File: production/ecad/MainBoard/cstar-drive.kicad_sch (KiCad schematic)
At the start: 55 parts, among them J1 B4B-PH-K-S, J2 B4B-PH-K-S, J3 Conn_01x03_Pin, J4 Conn_01x03_Pin, J5 Conn_01x03_Pin, J6 Conn_01x03_Pin, J7 Conn_01x03_Pin, J8 Conn_01x03_Pin, J9 Conn_01x03_Pin, U1 DRV8842PWPR, U2 DRV8842PWPR, X1 B2P-VH, X2 B2P-VH

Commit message: drive footprints (0805 C, R, connector pins)
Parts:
- C1, C10, C11, C12, C2, C3, C4, C5, C6, C7, C8, C9: footprint (none) -> Capacitor_SMD:C_0805_2012Metric
- J3, J4, J5, J6, J7, J8, J9: footprint (none) -> Connector_Phoenix_SPT:PhoenixContact_SPT_1.5_9-H-3.5_1x09_P3.5mm_Horizontal
- R1, R10, R2, R3, R4, R5, R6, R7, R8, R9: footprint (none) -> Resistor_SMD:R_0805_2012Metric

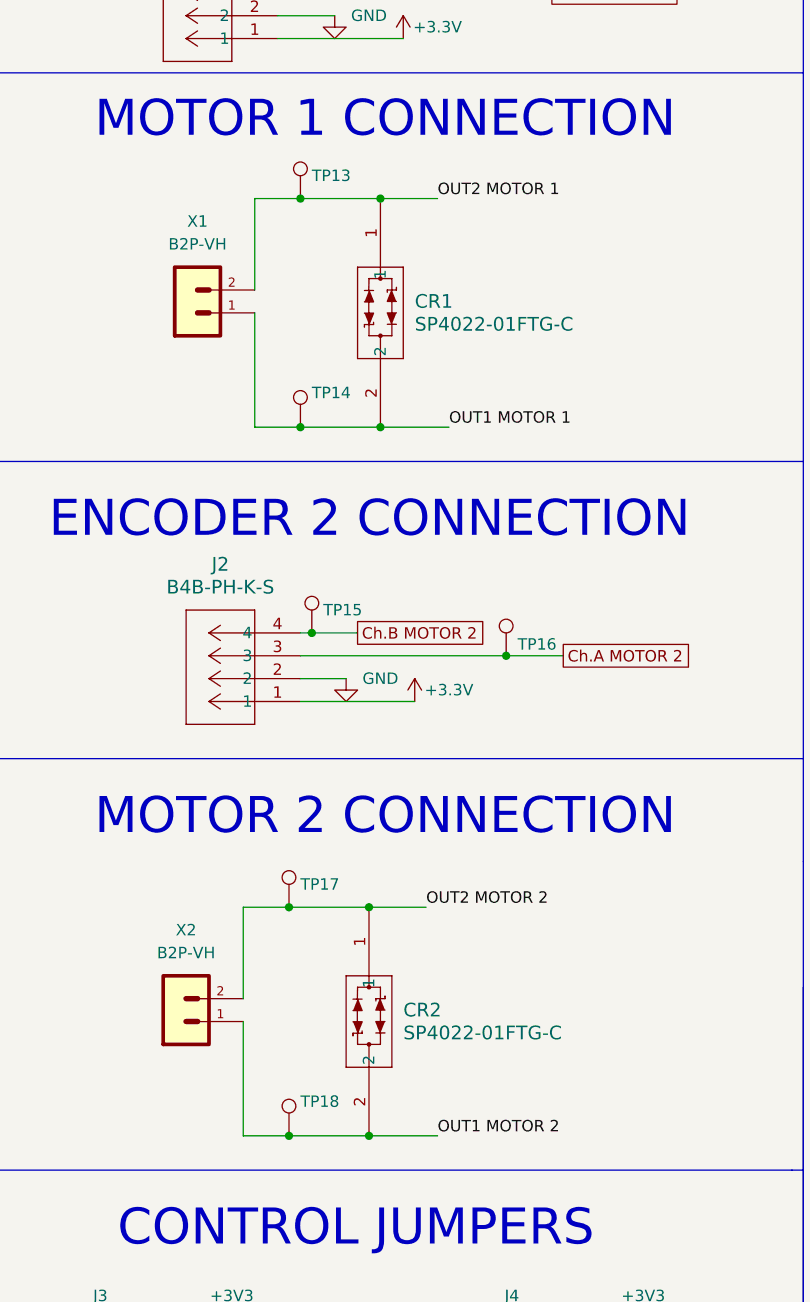
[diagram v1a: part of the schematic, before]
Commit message: "Added TP Footprints for drive"
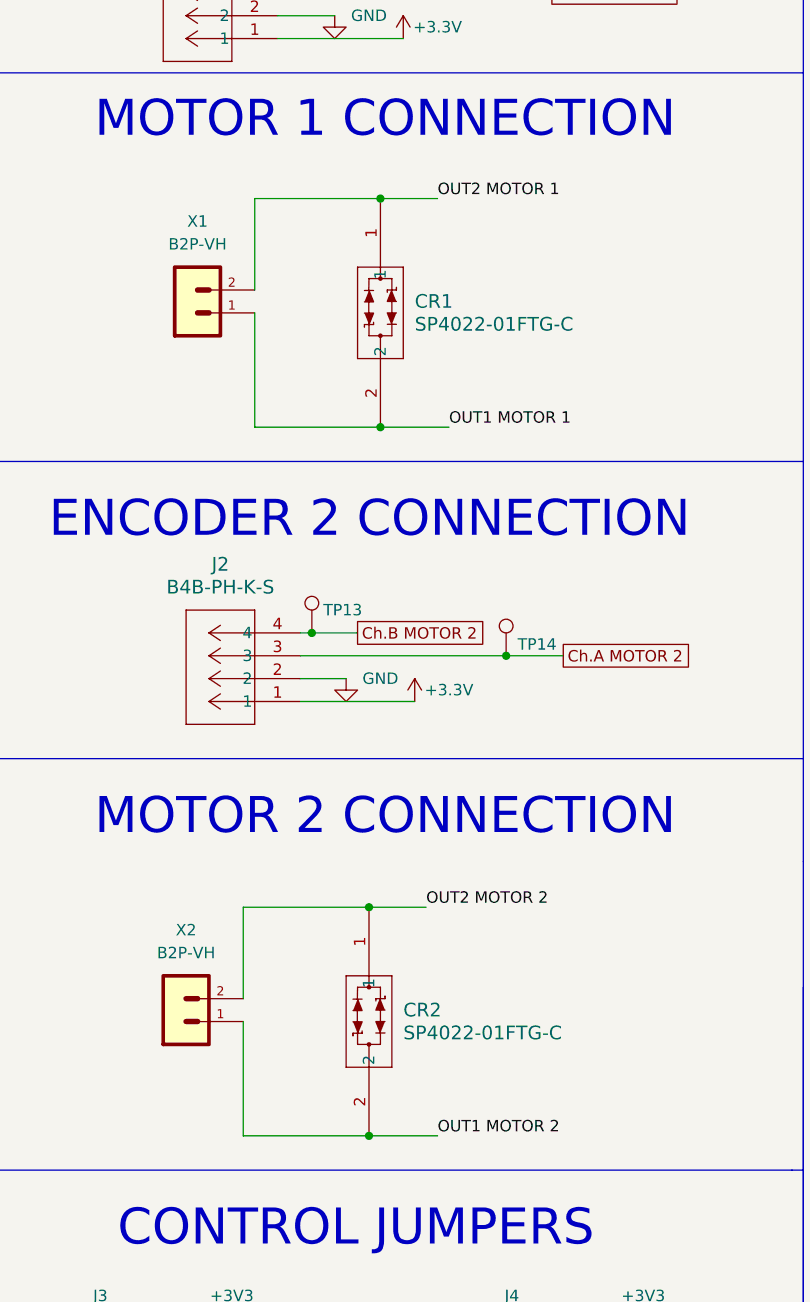
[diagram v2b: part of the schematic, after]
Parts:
- removed TP13, TP17: OUT2 MOTOR 1 TP, symbol Connector:TestPoint
- removed TP14, TP18: ~, symbol Connector:TestPoint
- TP1: footprint (none) -> TestPoint:TestPoint_Pad_D1.5mm
- TP10: value IN1 MOTOR 1 TP -> OUT2 MOTOR 2 TP; footprint (none) -> TestPoint:TestPoint_Pad_D1.5mm
- TP11: value TestPoint -> Ch.B MOTOR 1; footprint (none) -> TestPoint:TestPoint_Pad_D1.5mm
- TP12: value TestPoint -> Ch.A MOTOR 1; footprint (none) -> TestPoint:TestPoint_Pad_D1.5mm
- TP13: renamed from TP15; value TestPoint -> Ch.B MOTOR 2 TP; footprint (none) -> TestPoint:TestPoint_Pad_D1.5mm
- TP14: renamed from TP16; value TestPoint -> Ch.A MOTOR 2; footprint (none) -> TestPoint:TestPoint_Pad_D1.5mm
- TP2: value IN1 MOTOR 1 TP -> IN2 MOTOR 1 TP; footprint (none) -> TestPoint:TestPoint_Pad_D1.5mm; now left out of the parts list
- TP3: value IN1 MOTOR 1 TP -> nFAULT MOTOR 1 TP; footprint (none) -> TestPoint:TestPoint_Pad_D1.5mm
- TP4: value IN1 MOTOR 1 TP -> OUT1 MOTOR 1 TP; footprint (none) -> TestPoint:TestPoint_Pad_D1.5mm
- TP5: value IN1 MOTOR 1 TP -> OUT2 MOTOR 1 TP; footprint (none) -> TestPoint:TestPoint_Pad_D1.5mm
- TP6: value IN1 MOTOR 1 TP -> IN1 MOTOR 2 TP; footprint (none) -> TestPoint:TestPoint_Pad_D1.5mm
- TP7: value IN1 MOTOR 1 TP -> IN2 MOTOR 2 TP; footprint (none) -> TestPoint:TestPoint_Pad_D1.5mm
- TP8: value IN1 MOTOR 1 TP -> nFAULT MOTOR 2 TP; footprint (none) -> TestPoint:TestPoint_Pad_D1.5mm
- TP9: value IN1 MOTOR 1 TP -> OUT1 MOTOR 2 TP; footprint (none) -> TestPoint:TestPoint_Pad_D1.5mm

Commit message: "Added Footprints and Datasheets for all components in Drive Schematic"
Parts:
- CR1, CR2: footprint ZDO_SP4022_LTF -> SP4022_01FTG_C:ZDO_SP4022_LTF
- J1, J2: footprint CONN4_B4B-PH_JST -> B4B_PH_K_S:B4B_PH_K_S
- U1, U2: footprint PWP0028C_N -> DRV8842PWPR:PWP0028C_N
- X1, X2: footprint (none) -> B2P-VH:B2P-VH
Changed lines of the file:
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@@
       (effects (font (size 1.524 1.524)))
     )
-    (property "Footprint" "CONN4_B4B-PH_JST" (at 223.52 62.23 0)
+    (property "Footprint" "B4B_PH_K_S:B4B_PH_K_S" (at 223.52 62.23 0)
       (effects (font (size 1.27 1.27) italic) hide)
     )
-    (property "Datasheet" "B4B-PH-K-S" (at 223.52 62.23 0)
+    (property "Datasheet" "https://www.jst-mfg.com/product/pdf/eng/ePH.pdf" (at 223.52 62.23 0)
       (effects (font (size 1.27 1.27) italic) hide)
     )
@@
       (effects (font (size 1.524 1.524)) (justify left))
     )
-    (property "Footprint" "ZDO_SP4022_LTF" (at 233.68 158.75 0)
+    (property "Footprint" "SP4022_01FTG_C:ZDO_SP4022_LTF" (at 233.68 158.75 0)
       (effects (font (size 1.27 1.27) italic) hide)
     )
@@
       (effects (font (size 1.524 1.524)))
     )
-    (property "Footprint" "PWP0028C_N" (at 113.03 233.68 0)
+    (property "Footprint" "DRV8842PWPR:PWP0028C_N" (at 113.03 233.68 0)
       (effects (font (size 1.27 1.27) italic) hide)
     )
-    (property "Datasheet" "DRV8842PWPR" (at 113.03 233.68 0)
+    (property "Datasheet" "https://www.ti.com/lit/ds/symlink/drv8842.pdf?HQS=dis-dk-null-digikeymode-dsf-pf-null-wwe&ts=1708386124050" (at 113.03 233.68 0)
       (effects (font (size 1.27 1.27) italic) hide)
     )
@@
       (effects (font (size 1.524 1.524)) (justify left))
     )
-    (property "Footprint" "ZDO_SP4022_LTF" (at 234.95 80.01 0)
+    (property "Footprint" "SP4022_01FTG_C:ZDO_SP4022_LTF" (at 234.95 80.01 0)
       (effects (font (size 1.27 1.27) italic) hide)
     )
@@
       (effects (font (size 1.27 1.27)))
     )
-    (property "Footprint" "" (at 212.09 168.91 0)
-      (effects (font (size 1.27 1.27)) hide)
-    )
-    (property "Datasheet" "" (at 212.09 168.91 0)
+    (property "Footprint" "B2P-VH:B2P-VH" (at 212.09 168.91 0)
+      (effects (font (size 1.27 1.27)) hide)
+    )
+    (property "Datasheet" "https://www.jst-mfg.com/product/pdf/eng/eVH.pdf" (at 212.09 168.91 0)
       (effects (font (size 1.27 1.27)) hide)
     )
@@
       (effects (font (size 1.27 1.27)))
     )
-    (property "Footprint" "" (at 213.36 90.17 0)
-      (effects (font (size 1.27 1.27)) hide)
-    )
-    (property "Datasheet" "" (at 213.36 90.17 0)
+    (property "Footprint" "B2P-VH:B2P-VH" (at 213.36 90.17 0)
+      (effects (font (size 1.27 1.27)) hide)
+    )
+    (property "Datasheet" "https://www.jst-mfg.com/product/pdf/eng/eVH.pdf" (at 213.36 90.17 0)
       (effects (font (size 1.27 1.27)) hide)
     )
@@
       (effects (font (size 1.524 1.524)))
     )
-    (property "Footprint" "CONN4_B4B-PH_JST" (at 226.06 135.89 0)
+    (property "Footprint" "B4B_PH_K_S:B4B_PH_K_S" (at 226.06 135.89 0)
       (effects (font (size 1.27 1.27) italic) hide)
     )
-    (property "Datasheet" "B4B-PH-K-S" (at 226.06 135.89 0)
+    (property "Datasheet" "https://www.jst-mfg.com/product/pdf/eng/ePH.pdf" (at 226.06 135.89 0)
       (effects (font (size 1.27 1.27) italic) hide)
     )
@@
       (effects (font (size 1.524 1.524)))
     )
-    (property "Footprint" "PWP0028C_N" (at 111.76 114.3 0)
+    (property "Footprint" "DRV8842PWPR:PWP0028C_N" (at 111.76 114.3 0)
       (effects (font (size 1.27 1.27) italic) hide)
     )
-    (property "Datasheet" "DRV8842PWPR" (at 111.76 114.3 0)
+    (property "Datasheet" "https://www.ti.com/lit/ds/symlink/drv8842.pdf?HQS=dis-dk-null-digikeymode-dsf-pf-null-wwe&ts=1708386124050" (at 111.76 114.3 0)
       (effects (font (size 1.27 1.27) italic) hide)
     )

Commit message: "Updated Net Labels"
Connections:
- net Ch.A MOTOR 1 renamed Ch.A_MOTOR_1
- net Ch.A MOTOR 2 renamed Ch.A_MOTOR_2
- net Ch.B MOTOR 1 renamed Ch.B_MOTOR_1
- net Ch.B MOTOR 2 renamed Ch.B_MOTOR_2
- net IN1 MOTOR 1 renamed IN1_MOTOR_1
- net IN1 MOTOR 2 renamed IN1_MOTOR_2
- net IN2 MOTOR 1 renamed IN2_MOTOR_1
- net IN2 MOTOR 2 renamed IN2_MOTOR_2
- net OUT1 MOTOR 1 renamed OUT1_MOTOR_1
- net OUT1 MOTOR 2 renamed OUT1_MOTOR_2
- net OUT2 MOTOR 1 renamed OUT2_MOTOR_1
- net OUT2 MOTOR 2 renamed OUT2_MOTOR_2
- net nFAULT MOTOR 1 renamed nFAULT_MOTOR_1
- net nFAULT MOTOR 2 renamed nFAULT_MOTOR_2
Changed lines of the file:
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@@
     (stroke (width 0) (type default))
   )
-  (wire (pts (xy 227.33 128.27) (xy 232.41 128.27))
+  (wire (pts (xy 227.33 128.27) (xy 231.14 128.27))
     (stroke (width 0) (type default))
   )
@@
     (stroke (width 0) (type default))
   )
-  (wire (pts (xy 226.06 54.61) (xy 231.14 54.61))
+  (wire (pts (xy 226.06 54.61) (xy 229.87 54.61))
     (stroke (width 0) (type default))
   )
@@
     (effects (font (size 10 10) (thickness 2) bold) (justify left bottom))
   )
-  (label "OUT2 MOTOR 1" (at 241.3 80.01 0) (fields_autoplaced)
+  (label "OUT2_MOTOR_1" (at 241.3 80.01 0) (fields_autoplaced)
     (effects (font (size 1.27 1.27)) (justify left bottom))
   )
@@
     (effects (font (size 1.27 1.27)) (justify left bottom))
   )
-  (label "OUT2 MOTOR 2" (at 240.03 158.75 0) (fields_autoplaced)
+  (label "OUT2_MOTOR_2" (at 240.03 158.75 0) (fields_autoplaced)
     (effects (font (size 1.27 1.27)) (justify left bottom))
   )
@@
     (effects (font (size 1.27 1.27)) (justify left bottom))
   )
-  (label "OUT1 MOTOR 1" (at 143.51 93.98 0) (fields_autoplaced)
-    (effects (font (size 1.27 1.27)) (justify left bottom))
-  )
-  (label "OUT1 MOTOR 2" (at 241.3 184.15 0) (fields_autoplaced)
+  (label "OUT1_MOTOR_1" (at 143.51 93.98 0) (fields_autoplaced)
+    (effects (font (size 1.27 1.27)) (justify left bottom))
+  )
+  (label "OUT1_MOTOR_2" (at 241.3 184.15 0) (fields_autoplaced)
     (effects (font (size 1.27 1.27)) (justify left bottom))
   )
@@
     (effects (font (size 1.27 1.27)) (justify left bottom))
   )
-  (label "OUT1 MOTOR 1" (at 242.57 105.41 0) (fields_autoplaced)
-    (effects (font (size 1.27 1.27)) (justify left bottom))
-  )
-  (label "OUT2 MOTOR 2" (at 144.78 220.98 0) (fields_autoplaced)
+  (label "OUT1_MOTOR_1" (at 242.57 105.41 0) (fields_autoplaced)
+    (effects (font (size 1.27 1.27)) (justify left bottom))
+  )
+  (label "OUT2_MOTOR_2" (at 144.78 220.98 0) (fields_autoplaced)
     (effects (font (size 1.27 1.27)) (justify left bottom))
   )
@@
     (effects (font (size 1.27 1.27)) (justify left bottom))
   )
-  (label "OUT2 MOTOR 1" (at 143.51 101.6 0) (fields_autoplaced)
-    (effects (font (size 1.27 1.27)) (justify left bottom))
-  )
-  (label "OUT1 MOTOR 2" (at 144.78 213.36 0) (fields_autoplaced)
+  (label "OUT2_MOTOR_1" (at 143.51 101.6 0) (fields_autoplaced)
+    (effects (font (size 1.27 1.27)) (justify left bottom))
+  )
+  (label "OUT1_MOTOR_2" (at 144.78 213.36 0) (fields_autoplaced)
     (effects (font (size 1.27 1.27)) (justify left bottom))
   )
@@
     (effects (font (size 1.27 1.27)) (justify left bottom))
   )
-  (global_label "Ch.B MOTOR 1" (shape passive) (at 231.14 54.61 0) (fields_autoplaced)
+  (global_label "Ch.B_MOTOR_1" (shape input) (at 229.87 54.61 0) (fields_autoplaced)
     (effects (font (size 1.27 1.27)) (justify left))
-    (property "Intersheetrefs" "${INTERSHEET_REFS}" (at 246.8024 54.61 0)
+    (property "Intersheetrefs" "${INTERSHEET_REFS}" (at 246.6437 54.61 0)
       (effects (font (size 1.27 1.27)) (justify left) hide)
     )
   )
-  (global_label "nFAULT MOTOR 1" (shape passive) (at 58.42 144.78 180) (fields_autoplaced)
-    (effects (font (size 1.27 1.27)) (justify right))
-    (property "Intersheetrefs" "${INTERSHEET_REFS}" (at 40.399 144.78 0)
+  (global_label "nFAULT_MOTOR_1" (shape output) (at 58.42 144.78 180) (fields_autoplaced)
+    (effects (font (size 1.27 1.27)) (justify right))
+    (property "Intersheetrefs" "${INTERSHEET_REFS}" (at 39.2877 144.78 0)
       (effects (font (size 1.27 1.27)) (justify right) hide)
     )
   )
-  (global_label "nFAULT MOTOR 2" (shape passive) (at 59.69 264.16 180) (fields_autoplaced)
-    (effects (font (size 1.27 1.27)) (justify right))
-    (property "Intersheetrefs" "${INTERSHEET_REFS}" (at 41.669 264.16 0)
+  (global_label "nFAULT_MOTOR_2" (shape output) (at 59.69 264.16 180) (fields_autoplaced)
+    (effects (font (size 1.27 1.27)) (justify right))
+    (property "Intersheetrefs" "${INTERSHEET_REFS}" (at 40.5577 264.16 0)
       (effects (font (size 1.27 1.27)) (justify right) hide)
     )
   )
-  (global_label "Ch.A MOTOR 1" (shape passive) (at 254 57.15 0) (fields_autoplaced)
+  (global_label "Ch.A_MOTOR_1" (shape input) (at 254 57.15 0) (fields_autoplaced)
     (effects (font (size 1.27 1.27)) (justify left))
-    (property "Intersheetrefs" "${INTERSHEET_REFS}" (at 269.481 57.15 0)
+    (property "Intersheetrefs" "${INTERSHEET_REFS}" (at 270.5923 57.15 0)
       (effects (font (size 1.27 1.27)) (justify left) hide)
     )
   )
-  (global_label "Ch.B MOTOR 2" (shape passive) (at 232.41 128.27 0) (fields_autoplaced)
+  (global_label "Ch.B_MOTOR_2" (shape input) (at 231.14 128.27 0) (fields_autoplaced)
     (effects (font (size 1.27 1.27)) (justify left))
-    (property "Intersheetrefs" "${INTERSHEET_REFS}" (at 248.0724 128.27 0)
+    (property "Intersheetrefs" "${INTERSHEET_REFS}" (at 247.9137 128.27 0)
       (effects (font (size 1.27 1.27)) (justify left) hide)
     )
   )
-  (global_label "Ch.A MOTOR 2" (shape passive) (at 255.27 130.81 0) (fields_autoplaced)
+  (global_label "Ch.A_MOTOR_2" (shape input) (at 255.27 130.81 0) (fields_autoplaced)
     (effects (font (size 1.27 1.27)) (justify left))
-    (property "Intersheetrefs" "${INTERSHEET_REFS}" (at 270.751 130.81 0)
+    (property "Intersheetrefs" "${INTERSHEET_REFS}" (at 271.8623 130.81 0)
       (effects (font (size 1.27 1.27)) (justify left) hide)
     )
@@
     )
   )
-  (hierarchical_label "IN1 MOTOR 2" (shape passive) (at 83.82 223.52 180) (fields_autoplaced)
-    (effects (font (size 1.27 1.27)) (justify right))
-  )
-  (hierarchical_label "IN2 MOTOR 2" (shape passive) (at 83.82 228.6 180) (fields_autoplaced)
-    (effects (font (size 1.27 1.27)) (justify right))
-  )
-  (hierarchical_label "IN2 MOTOR 1" (shape passive) (at 82.55 109.22 180) (fields_autoplaced)
-    (effects (font (size 1.27 1.27)) (justify right))
-  )
-  (hierarchical_label "IN1 MOTOR 1" (shape passive) (at 82.55 104.14 180) (fields_autoplaced)
-    (effects (font (size 1.27 1.27)) (justify right))
-  )
+  (hierarchical_label "IN1_MOTOR_2" (shape passive) (at 83.82 223.52 180) (fields_autoplaced)
+    (effects (font (size 1.27 1.27)) (justify right))
+  )
+  (hierarchical_label "IN2_MOTOR_2" (shape passive) (at 83.82 228.6 180) (fields_autoplaced)
+    (effects (font (size 1.27 1.27)) (justify right))
+  )
+  (hierarchical_label "IN2_MOTOR_1" (shape passive) (at 82.55 109.22 180) (fields_autoplaced)
+    (effects (font (size 1.27 1.27)) (justify right))
+  )
+  (hierarchical_label "IN1_MOTOR_1" (shape passive) (at 82.55 104.14 180) (fields_autoplaced)
+    (effects (font (size 1.27 1.27)) (justify right))
+  )

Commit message: "Updated Jumper Footprints"
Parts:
- J3, J4, J5, J6, J7, J8, J9: footprint Connector_Phoenix_SPT:PhoenixContact_SPT_1.5_9-H-3.5_1x09_P3.5mm_Horizontal -> Connector_PinHeader_2.54mm:PinHeader_1x03_P2.54mm_Vertical
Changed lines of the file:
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@@
       (effects (font (size 1.27 1.27)))
     )
-    (property "Footprint" "Connector_Phoenix_SPT:PhoenixContact_SPT_1.5_9-H-3.5_1x09_P3.5mm_Horizontal" (at 248.92 209.55 0)
+    (property "Footprint" "Connector_PinHeader_2.54mm:PinHeader_1x03_P2.54mm_Vertical" (at 248.92 209.55 0)
       (effects (font (size 1.27 1.27)) hide)
     )
@@
       (effects (font (size 1.27 1.27)))
     )
-    (property "Footprint" "Connector_Phoenix_SPT:PhoenixContact_SPT_1.5_9-H-3.5_1x09_P3.5mm_Horizontal" (at 248.92 229.87 0)
+    (property "Footprint" "Connector_PinHeader_2.54mm:PinHeader_1x03_P2.54mm_Vertical" (at 248.92 229.87 0)
       (effects (font (size 1.27 1.27)) hide)
     )
@@
       (effects (font (size 1.27 1.27)))
     )
-    (property "Footprint" "Connector_Phoenix_SPT:PhoenixContact_SPT_1.5_9-H-3.5_1x09_P3.5mm_Horizontal" (at 228.6 267.97 0)
+    (property "Footprint" "Connector_PinHeader_2.54mm:PinHeader_1x03_P2.54mm_Vertical" (at 228.6 267.97 0)
       (effects (font (size 1.27 1.27)) hide)
     )
@@
       (effects (font (size 1.27 1.27)))
     )
-    (property "Footprint" "Connector_Phoenix_SPT:PhoenixContact_SPT_1.5_9-H-3.5_1x09_P3.5mm_Horizontal" (at 248.92 250.19 0)
+    (property "Footprint" "Connector_PinHeader_2.54mm:PinHeader_1x03_P2.54mm_Vertical" (at 248.92 250.19 0)
       (effects (font (size 1.27 1.27)) hide)
     )
@@
       (effects (font (size 1.27 1.27)))
     )
-    (property "Footprint" "Connector_Phoenix_SPT:PhoenixContact_SPT_1.5_9-H-3.5_1x09_P3.5mm_Horizontal" (at 203.2 209.55 0)
+    (property "Footprint" "Connector_PinHeader_2.54mm:PinHeader_1x03_P2.54mm_Vertical" (at 203.2 209.55 0)
       (effects (font (size 1.27 1.27)) hide)
     )
@@
       (effects (font (size 1.27 1.27)))
     )
-    (property "Footprint" "Connector_Phoenix_SPT:PhoenixContact_SPT_1.5_9-H-3.5_1x09_P3.5mm_Horizontal" (at 203.2 250.19 0)
+    (property "Footprint" "Connector_PinHeader_2.54mm:PinHeader_1x03_P2.54mm_Vertical" (at 203.2 250.19 0)
       (effects (font (size 1.27 1.27)) hide)
     )
@@
       (effects (font (size 1.27 1.27)))
     )
-    (property "Footprint" "Connector_Phoenix_SPT:PhoenixContact_SPT_1.5_9-H-3.5_1x09_P3.5mm_Horizontal" (at 203.2 229.87 0)
-      (effects (font (size 1.27 1.27)) hide)
-    )
+    (property "Footprint" "Connector_PinHeader_2.54mm:PinHeader_1x03_P2.54mm_Vertical" (at 203.2 229.87 0)
+      (effects (font (size 1.27 1.27)) hide)
+    )
